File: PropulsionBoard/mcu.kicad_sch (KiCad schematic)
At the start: 19 parts, among them J3 Programming Header, U11 PIC18F26K83, U12 MC2562, U5 PCA9536DR, Y1 Crystal

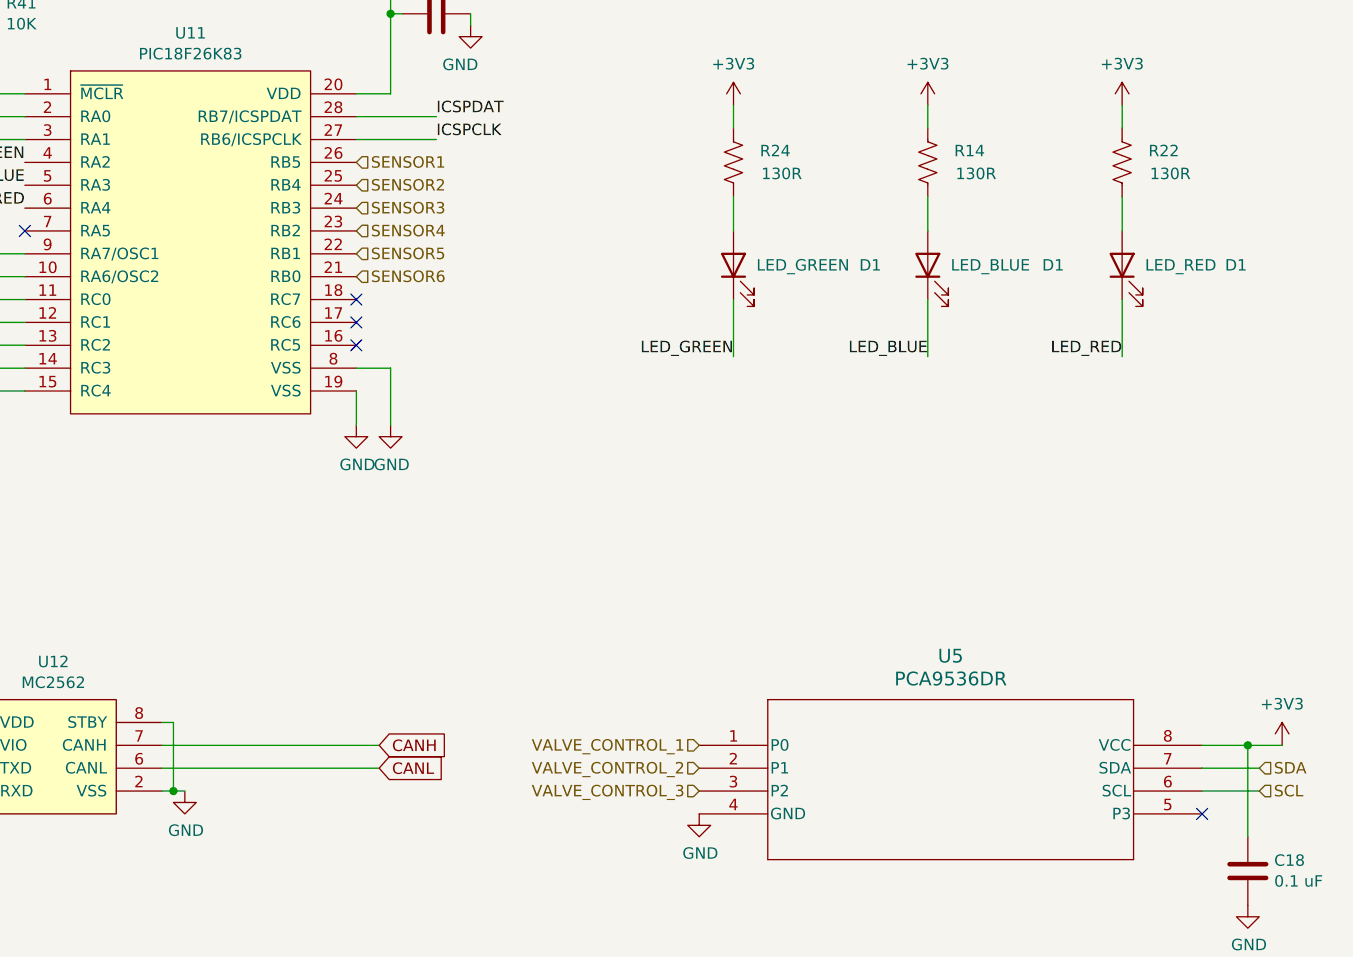
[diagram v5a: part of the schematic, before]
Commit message: propulsion board address fifth review changes
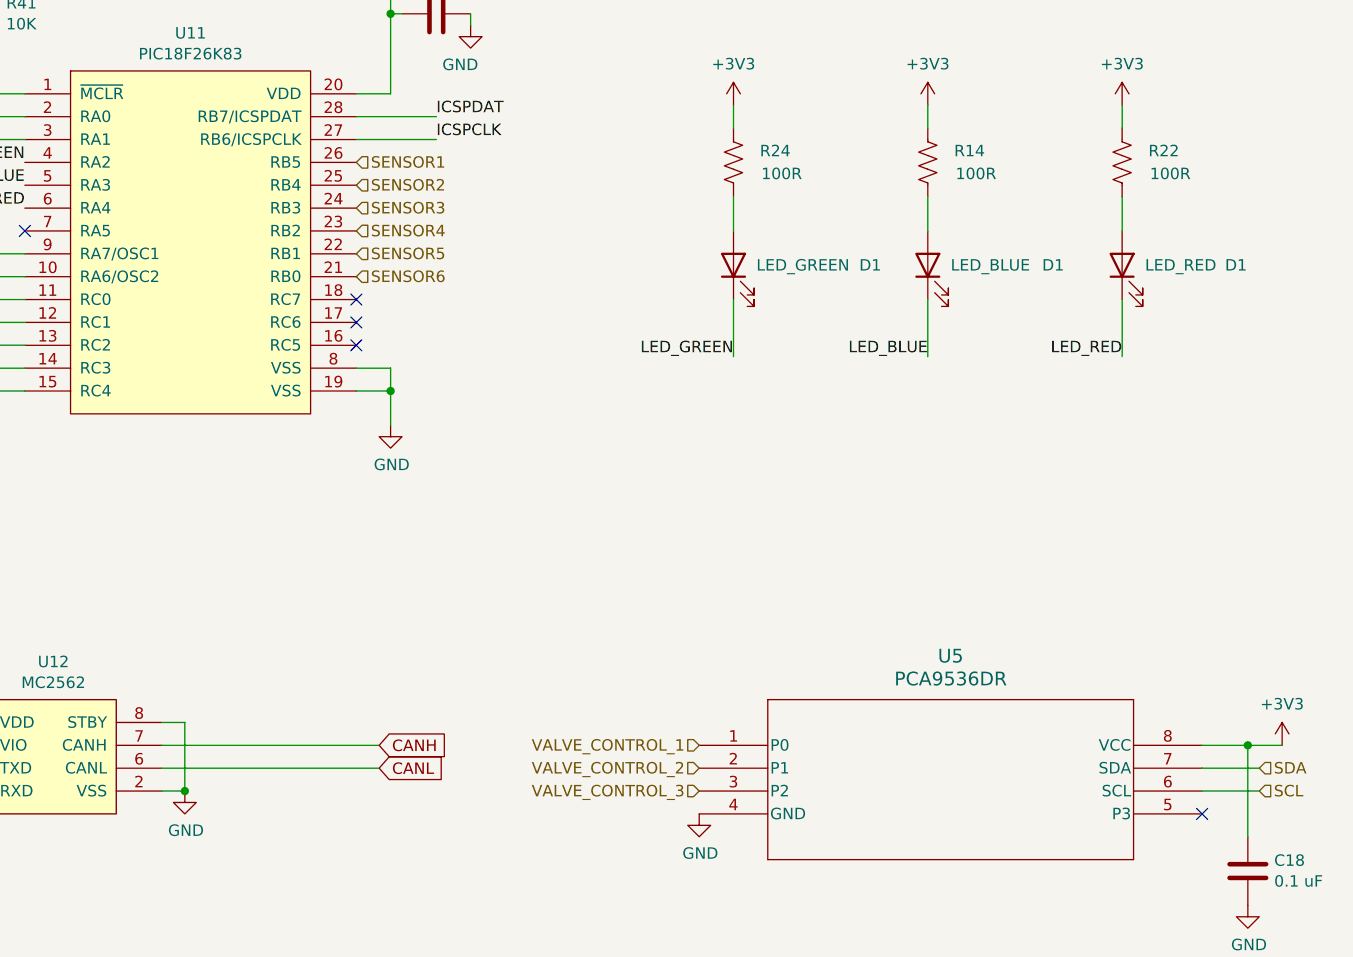
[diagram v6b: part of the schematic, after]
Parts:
- R14, R22, R24: value 130R -> 100R
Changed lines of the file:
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@@
   (junction (at 62.23 132.08) (diameter 0) (color 0 0 0 0)
   )
+  (junction (at 92.71 139.7) (diameter 0) (color 0 0 0 0)
+  )
+  (junction (at 115.57 95.25) (diameter 0) (color 0 0 0 0)
+  )
   (junction (at 251.46 82.55) (diameter 0) (color 0 0 0 0)
   )
@@
   )
   (junction (at 251.46 69.85) (diameter 0) (color 0 0 0 0)
-  )
-  (junction (at 91.44 139.7) (diameter 0) (color 0 0 0 0)
   )
   (junction (at 71.12 62.23) (diameter 0) (color 0 0 0 0)
@@
   (no_connect (at 111.76 90.17))
   (no_connect (at 205.74 142.24))
+  (wire (pts (xy 115.57 95.25) (xy 115.57 99.06))
+    (stroke (width 0) (type default))
+  )
   (wire (pts (xy 242.57 132.08) (xy 262.89 132.08))
     (stroke (width 0) (type default))
@@
     (stroke (width 0) (type default))
   )
+  (wire (pts (xy 111.76 95.25) (xy 115.57 95.25))
+    (stroke (width 0) (type default))
+  )
   (wire (pts (xy 227.33 77.47) (xy 227.33 76.2))
     (stroke (width 0) (type default))
@@
     (stroke (width 0) (type default))
   )
-  (wire (pts (xy 111.76 99.06) (xy 111.76 95.25))
-    (stroke (width 0) (type default))
-  )
   (wire (pts (xy 242.57 134.62) (xy 256.54 134.62))
     (stroke (width 0) (type default))
@@
     (stroke (width 0) (type default))
   )
-  (wire (pts (xy 91.44 139.7) (xy 92.71 139.7))
+  (wire (pts (xy 90.17 139.7) (xy 92.71 139.7))
     (stroke (width 0) (type default))
   )
@@
     (stroke (width 0) (type default))
   )
-  (wire (pts (xy 115.57 92.71) (xy 115.57 99.06))
+  (wire (pts (xy 115.57 92.71) (xy 115.57 95.25))
     (stroke (width 0) (type default))
   )
@@
     (stroke (width 0) (type default))
   )
-  (wire (pts (xy 90.17 139.7) (xy 91.44 139.7))
-    (stroke (width 0) (type default))
-  )
   (wire (pts (xy 67.31 80.01) (xy 74.93 80.01))
     (stroke (width 0) (type default))
@@
     (stroke (width 0) (type default))
   )
-  (wire (pts (xy 91.44 132.08) (xy 91.44 139.7))
+  (wire (pts (xy 92.71 132.08) (xy 92.71 139.7))
     (stroke (width 0) (type default))
   )
@@
     (stroke (width 0) (type default))
   )
-  (wire (pts (xy 90.17 132.08) (xy 91.44 132.08))
+  (wire (pts (xy 90.17 132.08) (xy 92.71 132.08))
     (stroke (width 0) (type default))
   )
@@
       (effects (font (size 1.27 1.27)) (justify left))
     )
-    (property "Value" "130R" (at 204.47 71.12 0)
+    (property "Value" "100R" (at 204.47 71.12 0)
       (effects (font (size 1.27 1.27)) (justify left))
     )
@@
       (effects (font (size 1.27 1.27)) (justify left))
     )
-    (property "Value" "130R" (at 161.29 71.12 0)
+    (property "Value" "100R" (at 161.29 71.12 0)
       (effects (font (size 1.27 1.27)) (justify left))
     )
@@
         (path "/d5641ac9-9be7-46bf-90b3-6c83d852b5ba/00000000-0000-0000-0000-00005bb1460e"
           (reference "R4") (unit 1)
-        )
-      )
-    )
-  )
-  (symbol (lib_id "power:GND") (at 111.76 99.06 0) (unit 1)
-    (in_bom yes) (on_board yes) (dnp no)
-    (property "Reference" "#PWR065" (at 111.76 105.41 0)
-      (effects (font (size 1.27 1.27)) hide)
-    )
-    (property "Value" "GND" (at 111.887 103.4542 0)
-      (effects (font (size 1.27 1.27)))
-    )
-    (property "Footprint" "" (at 111.76 99.06 0)
-      (effects (font (size 1.27 1.27)) hide)
-    )
-    (property "Datasheet" "" (at 111.76 99.06 0)
-      (effects (font (size 1.27 1.27)) hide)
-    )
-    (pin "1")
-    (instances
-      (project "Propulsion Board"
-        (path "/86ef6f38-2ca7-486c-b303-e50327233806/606d5b3a-2c24-4b65-aa9a-f6abe200f3e9"
-          (reference "#PWR065") (unit 1)
-        )
-        (path "/86ef6f38-2ca7-486c-b303-e50327233806/b71854ef-47d0-4ebc-9c0e-0ed7fdf34b23"
-          (reference "#PWR080") (unit 1)
-        )
-      )
-      (project "PropulsionBoard"
-        (path "/88c97d1e-364a-4c8a-b8a3-08e5c7306646/6f39ef58-4819-4dd9-bb07-efab959424e9"
-          (reference "#PWR044") (unit 1)
-        )
-      )
-      (project "sensors"
-        (path "/d5641ac9-9be7-46bf-90b3-6c83d852b5ba/00000000-0000-0000-0000-00005bb1460e"
-          (reference "#PWR06") (unit 1)
         )
       )
@@
       (effects (font (size 1.27 1.27)) (justify left))
     )
-    (property "Value" "130R" (at 182.88 71.12 0)
-      (effects (font (size 1.27 1.27)) (justify left))
-    )
+    (property "Value" "100R" (at 182.88 71.12 0)
+      (effects (font (size 1.27 1.27)) (justify left))
+    )

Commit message: latest progress of the propulsion board layout, but at last I got some issues on routing the 3.3V and GND and may need help for that
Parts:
- renumbered R24 to R4, R14 to R5, R22 to R6, U5 to U3
